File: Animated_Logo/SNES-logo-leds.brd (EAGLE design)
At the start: 22.9 x 19.7 mm, 9 parts

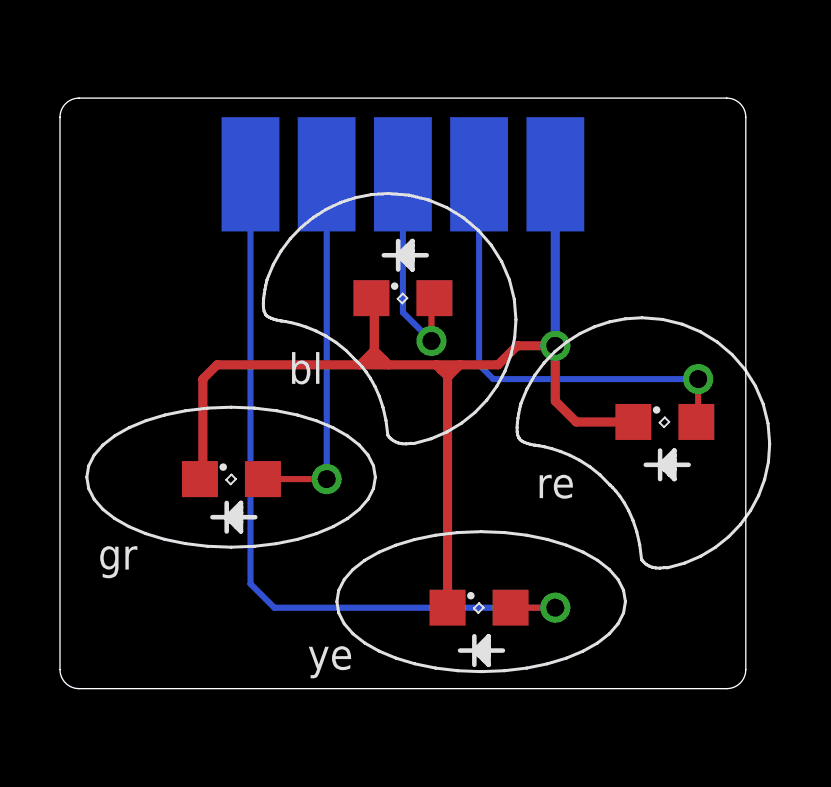
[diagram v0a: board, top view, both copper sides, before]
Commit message: Minor updates for the Logo-PCBs: - move resistors for LEDs to the LED PCB - LEDs can be either in 0805 or P-LCC-2 package
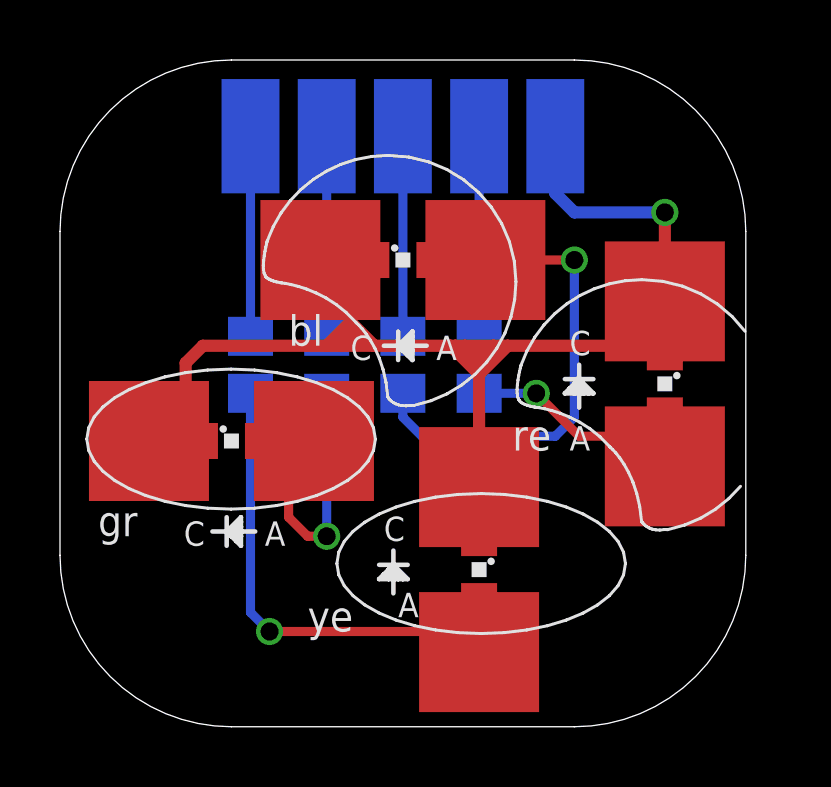
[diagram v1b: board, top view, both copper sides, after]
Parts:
- added LED5, LED6, LED7, LED8: (no value), led:P-LCC-2
- added R1, R2: 150, snes_div:Z0805
- added R3, R4: 100, snes_div:Z0805
- moved LED4 1.27 mm to (5.71, 8.26)
- moved LED1 1.27 mm to (14.0, 3.97), turned to 270 degrees
- moved LED2 1.27 mm to (20.2, 10.2), turned to 270 degrees
- moved LED3 1.27 mm to (11.4, 14.3)
- moved U$1 1.27 mm to (6.35, 18.4)
- moved U$3 1.27 mm to (14.0, 18.4)
- moved U$4 1.27 mm to (11.4, 18.4)
- moved U$5 1.27 mm to (8.89, 18.4)
- moved U$6 1.27 mm to (16.5, 18.4)
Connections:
- new net N$2: R2.1, U$3.P$1
- new net N$4: R1.1, U$1.P$1
- new net N$5: R3.1, U$4.P$1
- new net N$6: R4.1, U$5.P$1
- net N$1: now also LED5.C, LED6.C, LED7.C, LED8.C
- net N$20: now also LED6.A, R2.2; no longer U$3.P$1
- net N$21: now also LED7.A, R3.2; no longer U$4.P$1
- net N$22: now also LED8.A, R4.2; no longer U$5.P$1
- net N$3: now also LED5.A, R1.2; no longer U$1.P$1
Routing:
- net N$1: track 39.5 -> 50.9 mm
- net N$21: track 7.42 -> 16.9 mm
- net N$3: track 25.6 -> 18.8 mm
- net N$20: track 15.3 -> 8.48 mm
- net N$6: track 0.00 -> 6.67 mm
- net N$5: track 0.00 -> 6.67 mm
- net N$4: track 0.00 -> 6.67 mm
- net N$2: track 0.00 -> 6.67 mm
- net N$22: track 12.3 -> 10.5 mm
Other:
- board size 22.9 x 19.7 mm -> 22.9 x 22.2 mm
- board text added: "(adjust according to your LEDs used)"
- board text added: "180|2x120|180"
- board text added: "A"
- board text added: "C"
- board text added: "R1-R4:"
- board text added: "borti4938 __/)__/)_"
